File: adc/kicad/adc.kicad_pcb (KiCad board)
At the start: 2 copper layers, 90 x 88.4 mm, 115 parts, among them J1 Conn_01x07_Pin, J2 Conn_01x02_Pin, J3 Conn_01x02_Pin, J4 Conn_01x02_Pin, J5 pcie_98, U1 ADS1261BIRHBT, U2 ESD5344D-TP, U3 TPS7A2050PDBVR, U4 TPS7A2025PDBVRr, U6 TPS65135, U7 ADP7182AUJZ-5.0, U8 ADP7182AUJZ-2.5, U9 XC6206P332MR

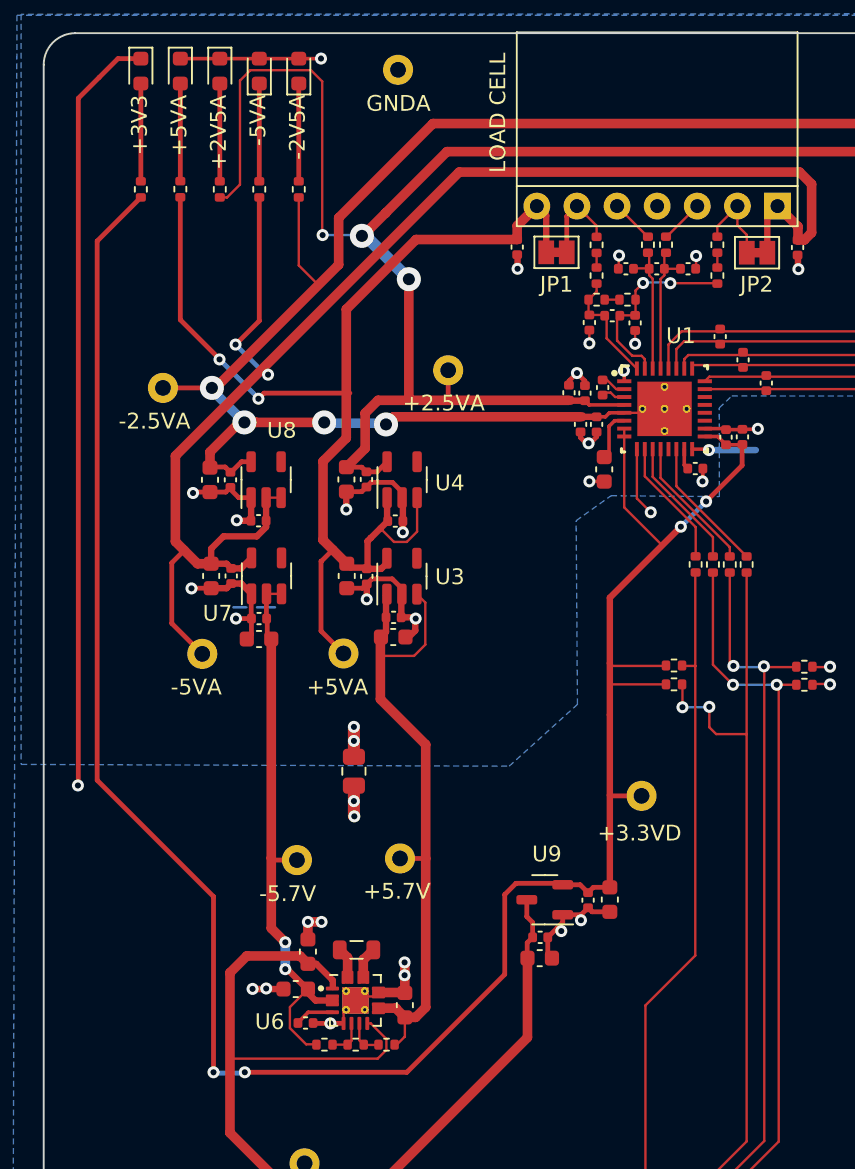
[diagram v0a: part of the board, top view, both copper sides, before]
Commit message: Replaced ADC DC/DC inductor with a higher current one.
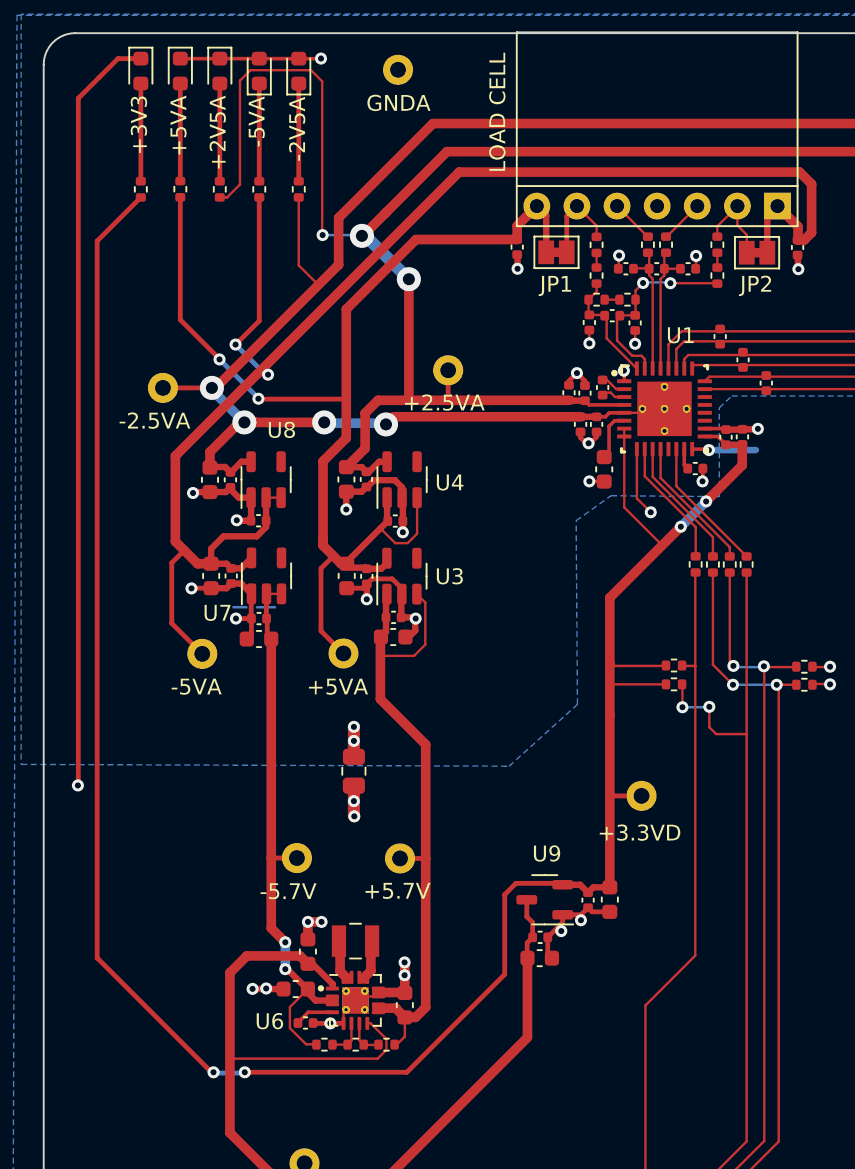
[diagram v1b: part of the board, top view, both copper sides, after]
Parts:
- L1: footprint Inductor_SMD:L_0805_2012Metric -> adc:Inductor_C329578
- R23, R24: value 5K1 -> 10K
- moved L1 0.56 mm to (-8.41, -30.9)
- moved TP4 0.13 mm to (-12.1, -36.2)

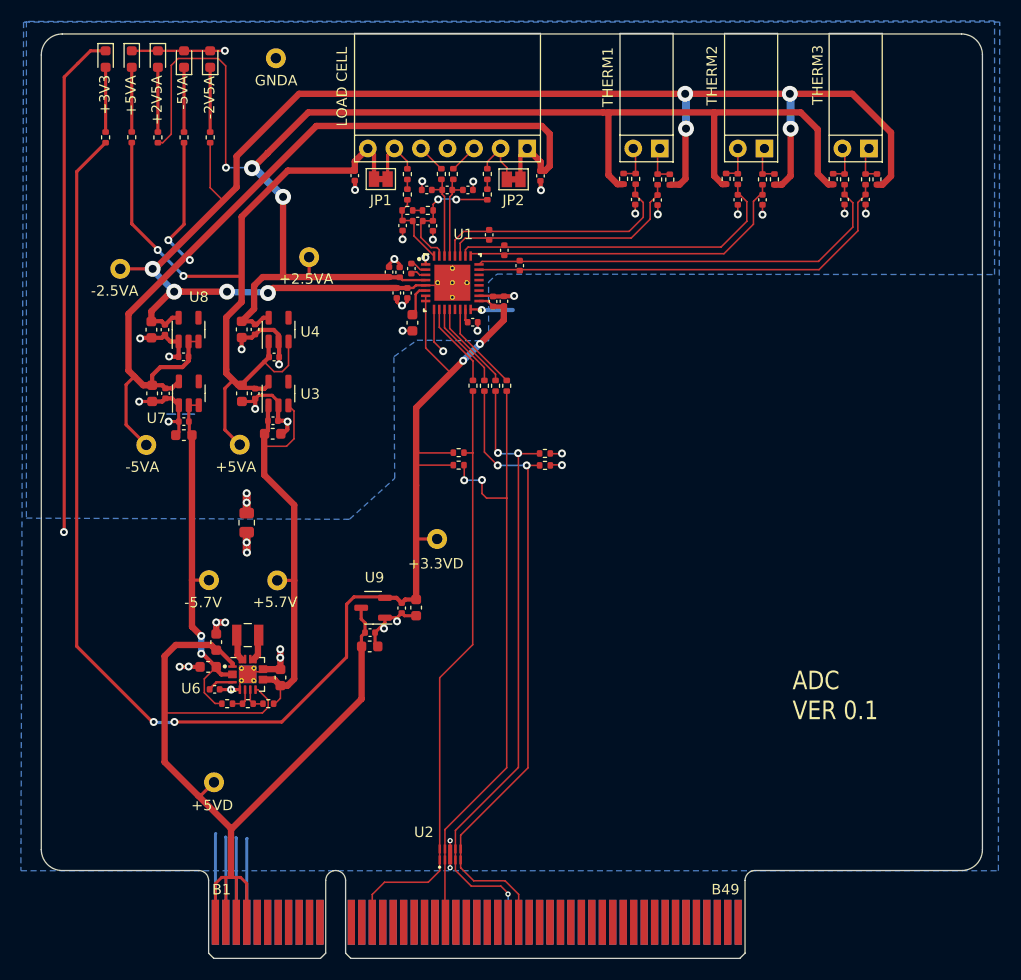
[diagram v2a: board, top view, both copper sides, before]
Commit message: Fixed library pathes and bus pin number.
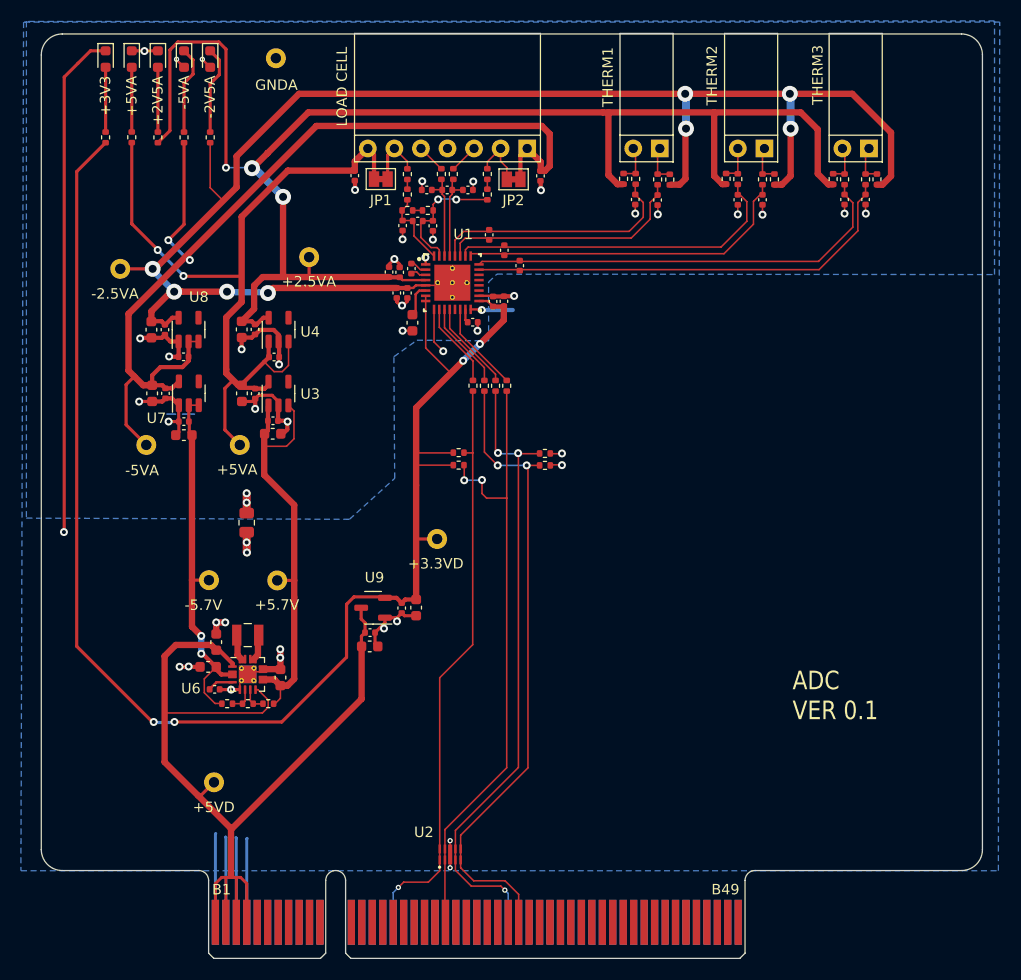
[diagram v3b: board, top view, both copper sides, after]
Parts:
- turned D2 to -90 degrees
- turned D4 to -90 degrees
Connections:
- J5 pad A16: unconnected-(J5-Pin_a16-PadA16) -> /PB14
- J5 pad B14: /PB14 -> unconnected-(J5-Pin_b14-PadB14)
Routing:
- net GNDA: track 61.5 -> 57.2 mm, vias 28 -> 30
- net /+2V5A: track 142.1 -> 145.0 mm
- net Net-(D4-K): track 6.19 -> 8.49 mm
- net Net-(D2-K): track 6.19 -> 8.48 mm
- net /PB14: track 58.1 -> 56.2 mm, vias 0 -> 1

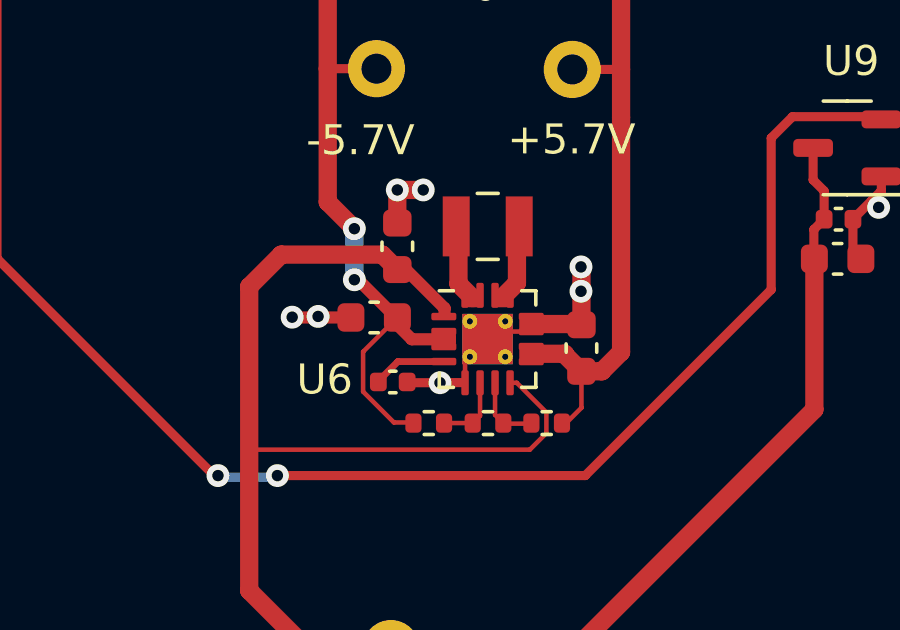
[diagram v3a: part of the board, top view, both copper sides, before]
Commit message: Changed LED to green and used DC/DC footprint with longer pads for manual soldering.
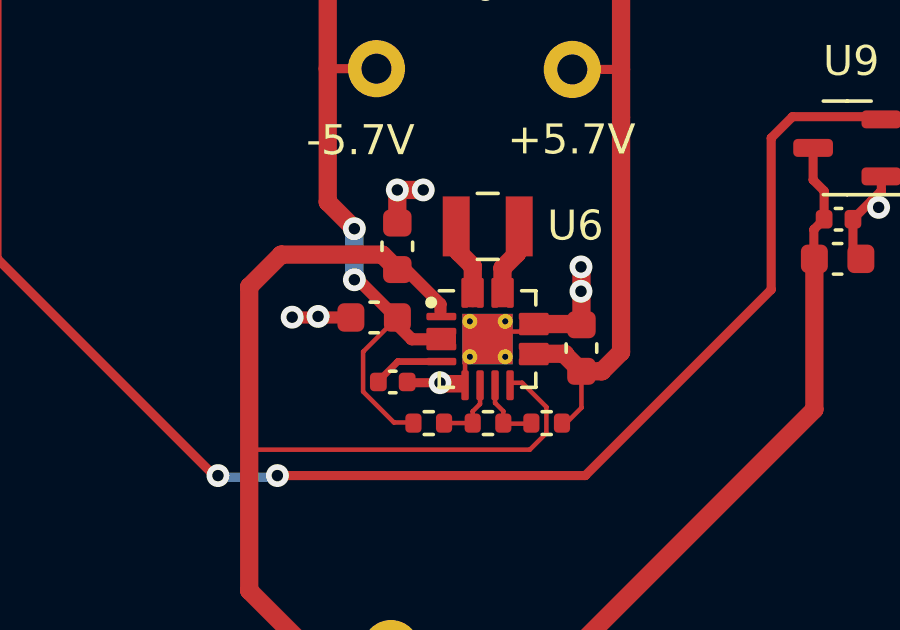
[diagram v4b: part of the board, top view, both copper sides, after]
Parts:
- U6: footprint Package_DFN_QFN:WQFN-16-1EP_3x3mm_P0.5mm_EP1.68x1.68mm_ThermalVias -> adc:WQFN-16-1EP_3x3mm_P0.5mm_EP1.68x1.68mm_ThermalVias
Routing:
- net GNDD: track 118.0 -> 119.7 mm

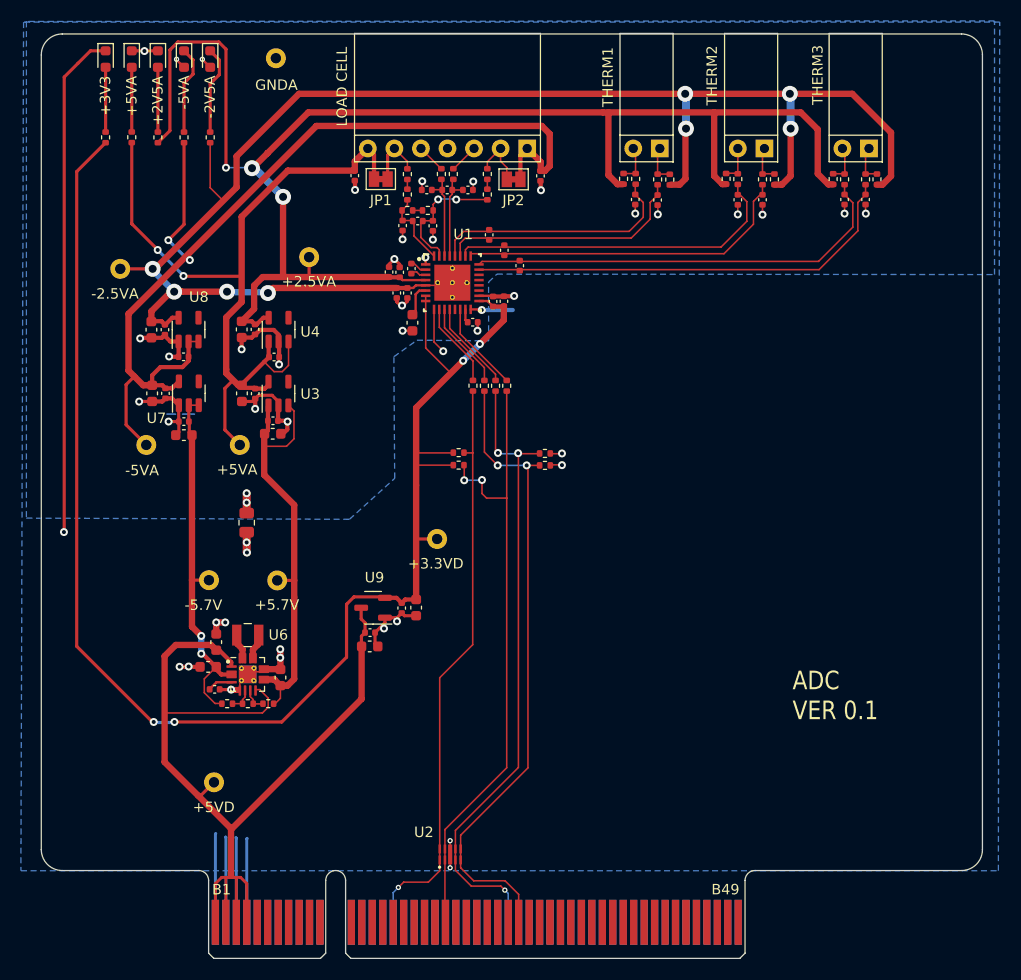
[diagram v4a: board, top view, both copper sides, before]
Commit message: Clenaed up ADC TODOs. Changed DC/DC resistors from 0.1% to 1% and merged grounds.
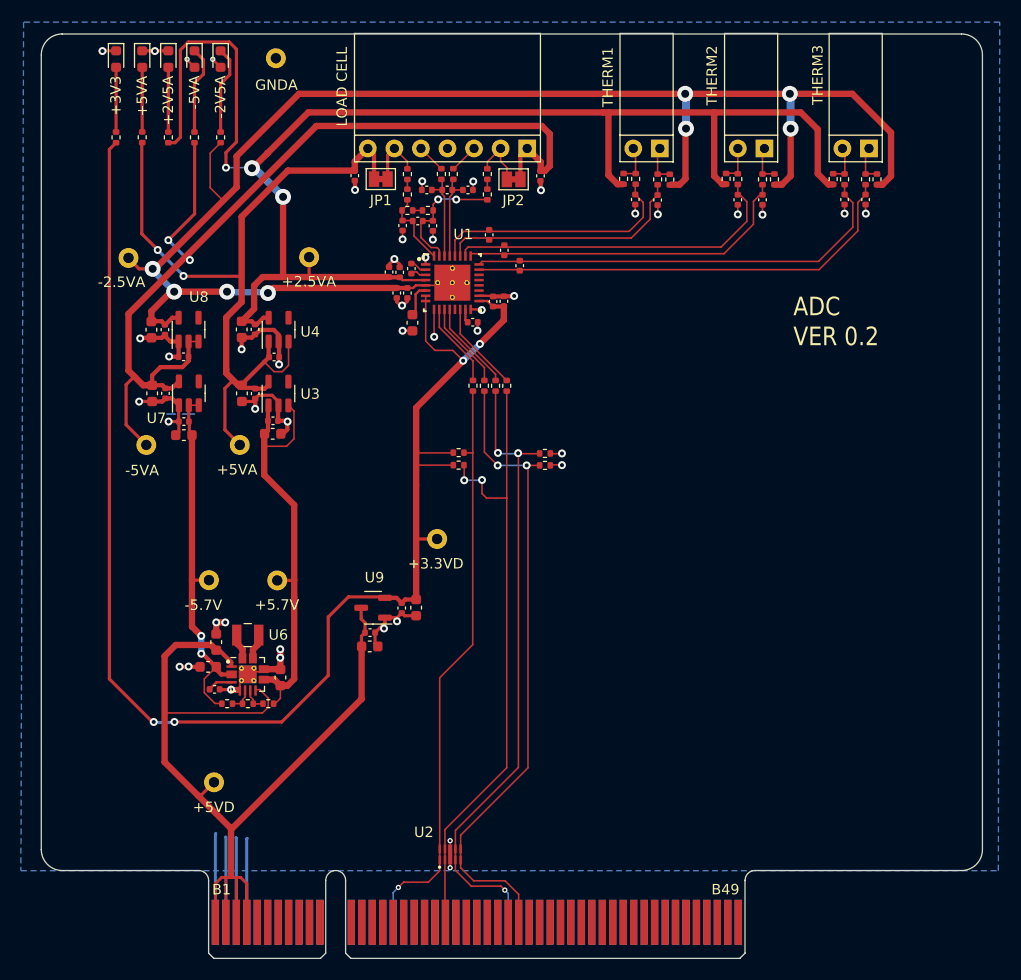
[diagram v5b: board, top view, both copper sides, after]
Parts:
- removed R37: 0R, Resistor_SMD:R_0805_2012Metric
- D1, D2, D3, D4, D5: value RED -> GRN
- R31: value 360K 0.1% -> 360K 1%
- R32: value 100K 0.1% -> 100K 1%
- R33: value 464K 0.1% -> 464K 1%
- moved TP8 1.31 mm to (-19.8, -67.0)
- moved D1 1.00 mm to (-18.5, -86.0)
- moved D2 1.00 mm to (-13.5, -86.0)
- moved D3 1.00 mm to (-16.0, -86.0)
- moved D4 1.00 mm to (-11.0, -86.0)
- moved D5 1.00 mm to (-21.0, -86.0)
- moved R23 1.00 mm to (-18.5, -78.5)
- moved R24 1.00 mm to (-13.5, -78.5)
- moved R25 1.00 mm to (-16.0, -78.5)
- moved R26 1.00 mm to (-11.0, -78.5)
- moved R27 1.00 mm to (-21.0, -78.5)
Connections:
- C10 pad 1: GNDA -> GND
- C11 pad 2: GNDD -> GND
- C12 pad 1: GNDA -> GND
- C13 pad 2: GNDD -> GND
- C14 pad 2: GNDA -> GND
- C16 pad 1: GNDA -> GND
- C18 pad 2: GNDA -> GND
- C2 pad 1: GNDA -> GND
- C20 pad 1: GNDA -> GND
- C21 pad 2: GNDA -> GND
- C22 pad 2: GNDA -> GND
- C23 pad 1: GNDA -> GND
- C24 pad 1: GNDA -> GND
- C25 pad 1: GNDA -> GND
- C26 pad 1: GNDA -> GND
- C27 pad 1: GNDA -> GND
- C28 pad 1: GNDA -> GND
- C29 pad 1: GNDD -> GND
- C3 pad 1: GNDA -> GND
- C30 pad 1: GNDD -> GND
- C31 pad 1: GNDD -> GND
- C32 pad 1: GNDD -> GND
- C33 pad 2: GNDD -> GND
- C34 pad 1: GNDA -> GND
- C35 pad 1: GNDA -> GND
- C36 pad 1: GNDA -> GND
- C37 pad 1: GNDA -> GND
- C38 pad 1: GNDA -> GND
- C39 pad 1: GNDA -> GND
- C4 pad 2: GNDA -> GND
- C40 pad 1: GNDA -> GND
- C41 pad 1: GNDD -> GND
- C42 pad 2: GNDD -> GND
- C43 pad 2: GNDD -> GND
- C44 pad 1: GNDA -> GND
- C45 pad 1: GNDA -> GND
- C46 pad 2: GNDA -> GND
- C47 pad 2: GNDA -> GND
- C48 pad 1: GNDA -> GND
- C7 pad 1: GNDA -> GND
- C8 pad 2: GNDA -> GND
- C9 pad 2: GNDA -> GND
- D1 pad 1: GNDA -> GND
- D2 pad 2: GNDA -> GND
- D3 pad 1: GNDA -> GND
- D4 pad 2: GNDA -> GND
- D5 pad 1: GNDD -> GND
- J1 pad 4: GNDA -> GND
- J5 pad A1: GNDD -> GND
- J5 pad A2: GNDD -> GND
- J5 pad A3: GNDD -> GND
- J5 pad A4: GNDD -> GND
- R28 pad 1: GNDD -> GND
- R29 pad 1: GNDD -> GND
- TP1 pad 1: GNDA -> GND
- U1 pad 1: GNDA -> GND
- U1 pad 16: GNDD -> GND
- U1 pad 18: GNDD -> GND
- U1 pad 9: GNDD -> GND
- U2 pad 3: GNDD -> GND
- U3 pad 2: GNDA -> GND
- U4 pad 2: GNDA -> GND
- U6 pad 11: GNDD -> GND
- U6 pad 12: GNDD -> GND
- U6 pad 17: GNDD -> GND
- U6 pad 5: GNDD -> GND
- U7 pad 1: GNDA -> GND
- U8 pad 1: GNDA -> GND
- U9 pad 1: GNDD -> GND
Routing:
- net GND: track 0.00 -> 121.2 mm, vias 0 -> 45
- net GNDD: track 119.7 -> 0.00 mm, vias 19 -> 0
- net GNDA: track 57.2 -> 0.00 mm, vias 30 -> 0
- net /+3V3D: track 144.1 -> 142.6 mm
- net /+2V5A: track 145.0 -> 145.8 mm
- added copper zone on B.Cu, net GND
- removed copper zone on B.Cu, net GNDA
- removed copper zone on B.Cu, net GNDD
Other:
- board text added: "ADC VER 0.2"
- board text removed: "ADC VER 0.1"
